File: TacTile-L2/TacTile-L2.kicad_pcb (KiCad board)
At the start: 2 copper layers, 3 parts, among them J1 Conn_01x05, J2 Conn_01x05, U1 74HC595

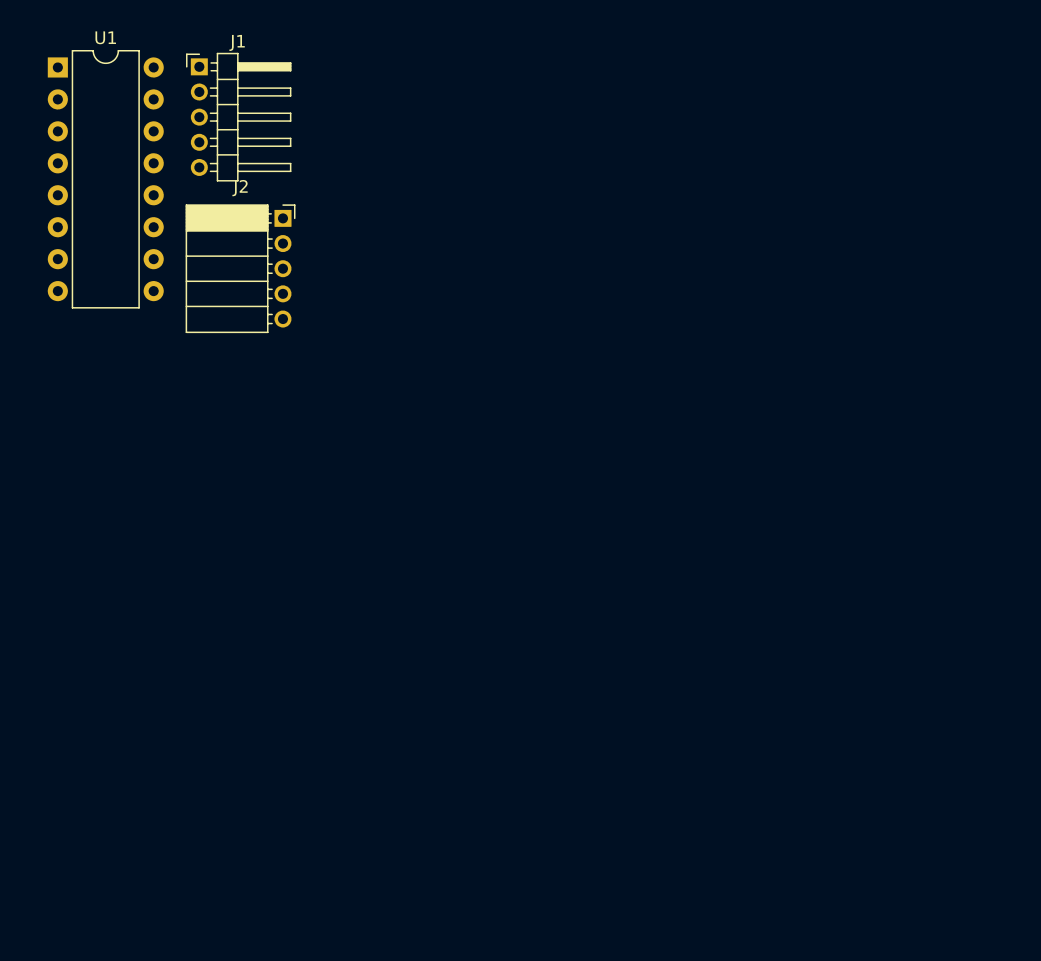
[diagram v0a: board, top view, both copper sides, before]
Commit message: Added photoresistor footprint and enlarged main boards to 60mm
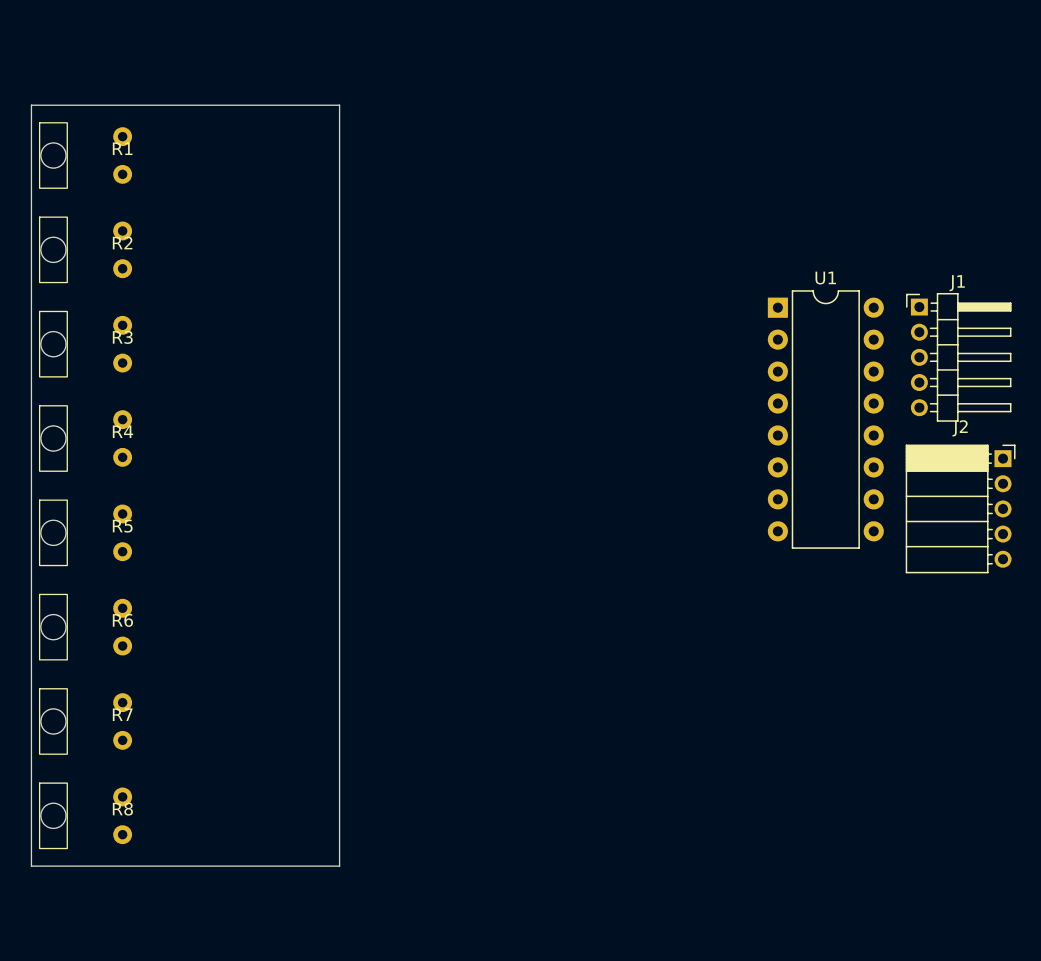
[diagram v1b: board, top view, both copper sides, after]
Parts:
- added R1: R_Photo, TacTile:Photoresistor, F.Cu at (32.2, 29.0)
- added R2: R_Photo, TacTile:Photoresistor, F.Cu at (32.2, 36.5)
- added R3: R_Photo, TacTile:Photoresistor, F.Cu at (32.2, 44.0)
- added R4: R_Photo, TacTile:Photoresistor, F.Cu at (32.2, 51.5)
- added R5: R_Photo, TacTile:Photoresistor, F.Cu at (32.2, 59.0)
- added R6: R_Photo, TacTile:Photoresistor, F.Cu at (32.2, 66.5)
- added R7: R_Photo, TacTile:Photoresistor, F.Cu at (32.2, 74.0)
- added R8: R_Photo, TacTile:Photoresistor, F.Cu at (32.2, 81.5)
- moved J2 60.4 mm to (102.2, 53.1)
- moved J1 60.4 mm to (95.6, 41.0)
- moved U1 60.4 mm to (84.3, 41.1)
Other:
- board outline added: 24.5 x 60.5 mm

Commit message: Finished L2 Board
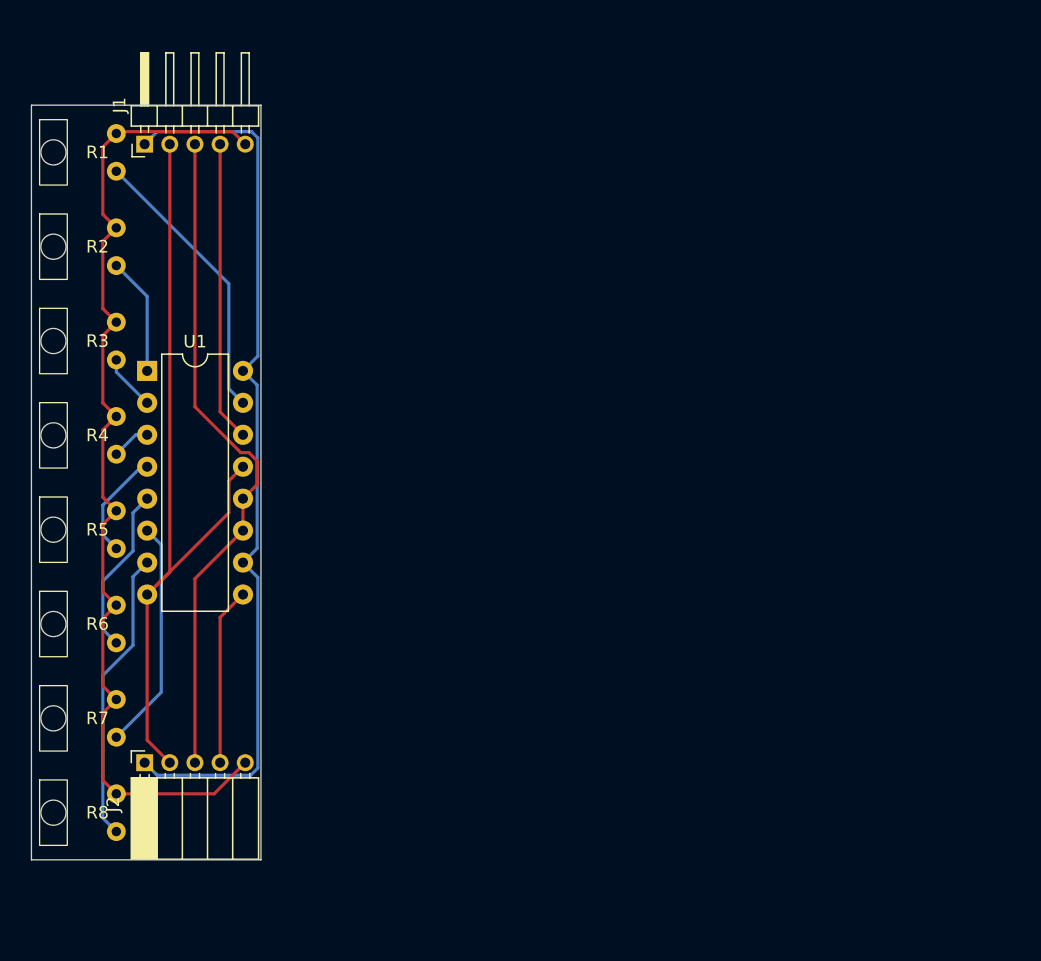
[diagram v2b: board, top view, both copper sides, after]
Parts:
- moved J2 72.4 mm to (34.0, 77.3), turned to 90 degrees
- moved J1 62.9 mm to (34.0, 28.1), turned to 90 degrees
- moved U1 50.4 mm to (34.2, 46.1)
- moved R1 5.51 mm to (26.8, 28.8)
- moved R2 5.51 mm to (26.8, 36.2)
- moved R3 5.51 mm to (26.8, 43.8)
- moved R4 5.51 mm to (26.8, 51.2)
- moved R5 5.51 mm to (26.8, 58.8)
- moved R6 5.51 mm to (26.8, 66.2)
- moved R7 5.51 mm to (26.8, 73.8)
- moved R8 5.51 mm to (26.8, 81.2)
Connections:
- J2 pad 1: /OUT -> /VCC
- J2 pad 2: /SOUT -> /GND
- J2 pad 4: /GND -> /SOUT
- J2 pad 5: /VCC -> /OUT
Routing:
- net /OUT: track 0.00 -> 80.7 mm
- net /VCC: track 0.00 -> 71.3 mm
- net /GND: track 0.00 -> 64.0 mm
- net /CLK: track 0.00 -> 53.7 mm
- net /SIN: track 0.00 -> 23.9 mm
- net Net-(U1-QH): track 0.00 -> 23.3 mm
- net Net-(U1-QA): track 0.00 -> 22.6 mm
- net Net-(U1-QG): track 0.00 -> 18.4 mm
- net /SOUT: track 0.00 -> 14.1 mm
- net Net-(U1-QF): track 0.00 -> 13.4 mm
- net Net-(U1-QB): track 0.00 -> 9.39 mm
- net Net-(U1-QE): track 0.00 -> 8.68 mm
- net Net-(U1-QC): track 0.00 -> 4.43 mm
- net Net-(U1-QD): track 0.00 -> 3.09 mm
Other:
- board size 24.5 x 60.5 mm -> 18.2 x 60 mm

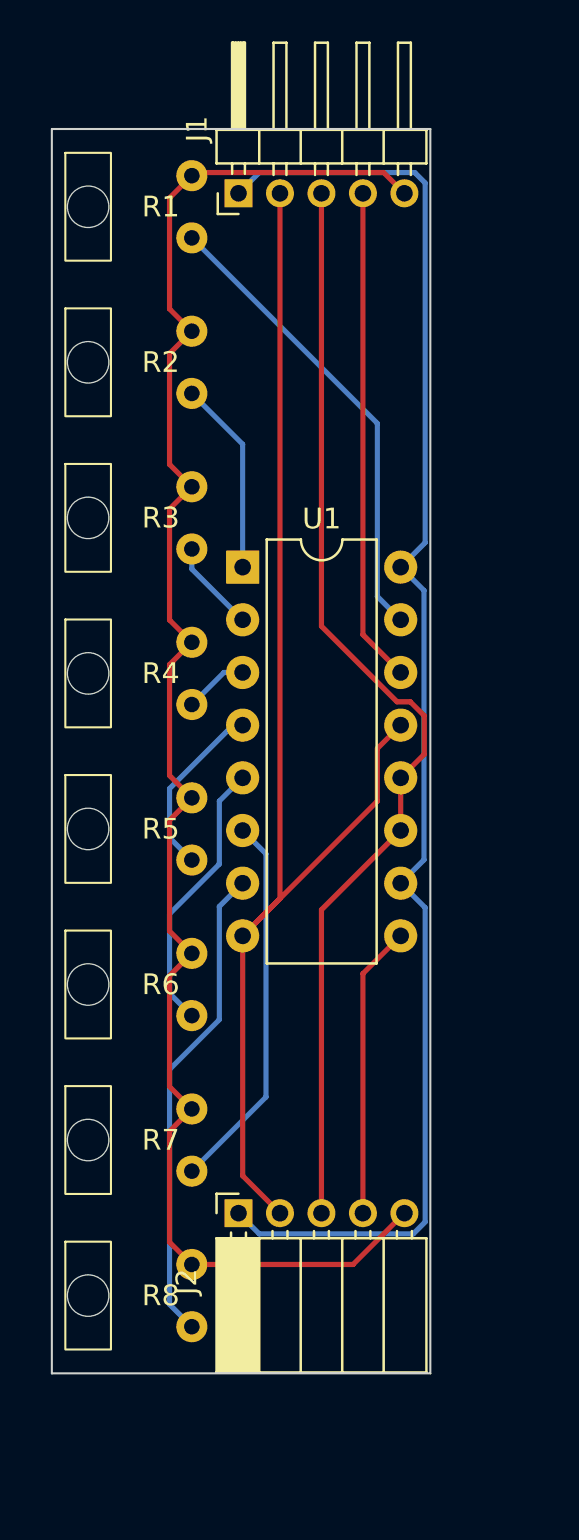
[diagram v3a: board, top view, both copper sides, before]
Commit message: Finished enlarging pins on C, D, L1, L2
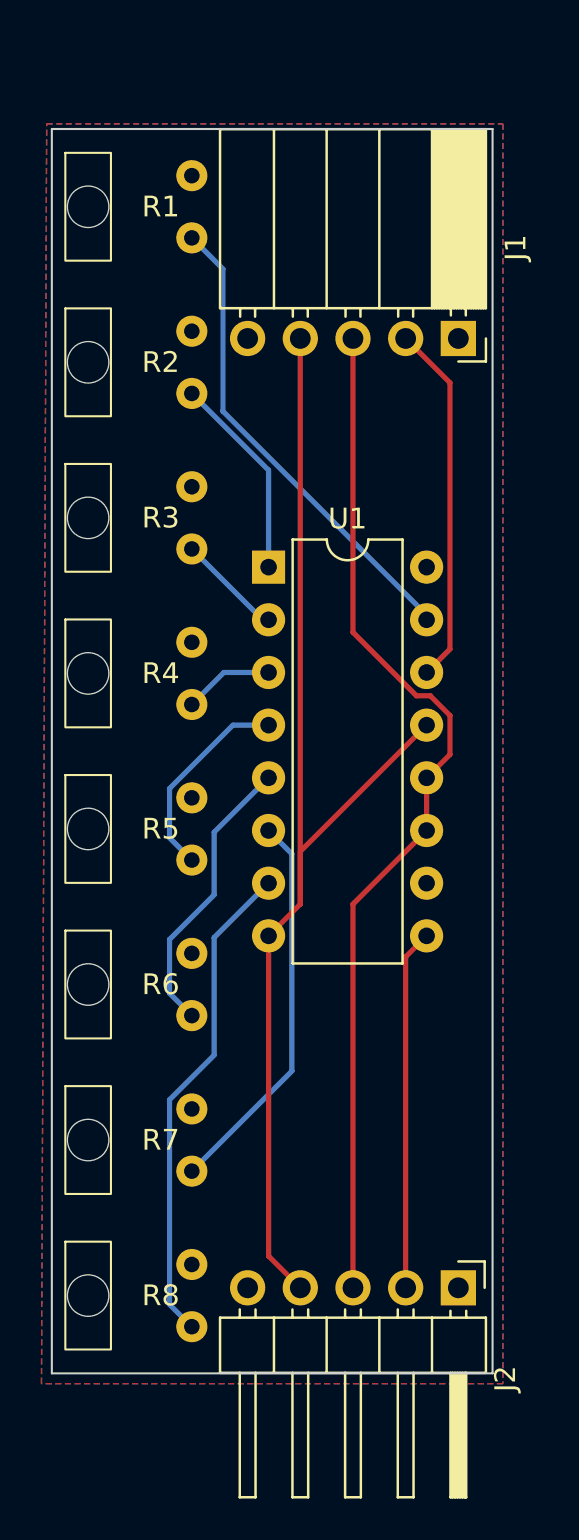
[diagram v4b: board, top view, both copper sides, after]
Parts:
- J1: footprint Connector_PinHeader_2.00mm:PinHeader_1x05_P2.00mm_Horizontal -> Connector_PinSocket_2.54mm:PinSocket_1x05_P2.54mm_Horizontal
- J2: footprint Connector_PinSocket_2.00mm:PinSocket_1x05_P2.00mm_Horizontal -> Connector_PinHeader_2.54mm:PinHeader_1x05_P2.54mm_Horizontal
- moved J1 12.7 mm to (44.6, 35.1), turned to -90 degrees
- moved J2 11.2 mm to (44.6, 80.9), turned to -90 degrees
- moved U1 1.25 mm to (35.5, 46.1)
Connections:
- J1 pad 1: /VCC -> /OUT
- J1 pad 2: /GND -> /SIN
- J1 pad 4: /SIN -> /GND
- J1 pad 5: /OUT -> /VCC
- J2 pad 1: /VCC -> /OUT
- J2 pad 2: /GND -> /SOUT
- J2 pad 4: /SOUT -> /GND
- J2 pad 5: /OUT -> /VCC
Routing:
- net /OUT: track 80.7 -> 0.00 mm
- net /VCC: track 71.3 -> 0.00 mm
- net /SIN: track 23.9 -> 17.5 mm
- net /GND: track 64.0 -> 58.2 mm
- net /CLK: track 53.7 -> 50.0 mm
- net /SOUT: track 14.1 -> 17.4 mm
- net Net-(U1-QE): track 8.68 -> 9.93 mm
- net Net-(U1-QD): track 3.09 -> 4.34 mm
- net Net-(U1-QC): track 4.43 -> 5.11 mm
- net Net-(U1-QA): track 22.6 -> 23.1 mm
- net Net-(U1-QH): track 23.3 -> 23.8 mm
- net Net-(U1-QG): track 18.4 -> 18.9 mm
- net Net-(U1-QF): track 13.4 -> 13.9 mm
- net Net-(U1-QB): track 9.39 -> 9.91 mm
- added copper zone on F.Cu, net /OUT
- added copper zone on B.Cu, net /VCC
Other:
- board size 18.2 x 60 mm -> 21.2 x 60 mm
